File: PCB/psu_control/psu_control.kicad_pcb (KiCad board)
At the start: 4 copper layers, 100 x 70 mm, 113 parts, among them J1 Vin (10-25V), J10 Other 1 I2C, J11 Light Sensor Front, J12 Light Sensor Left, J13 Light Sensor Back, J14 Light Sensor Right, J15 RRC-PMM240, J16 RS232, J2 Vout (10-25V), J3 Vout (5V), J4 Vout (10-25V), J6 LED Strip, J7 Amplifier 2 I2C, J8 Amplifier 1 I2C, J9 Amplifier 2 I2C, M1 Fan, M2 Fan, Q1 SSM3J372R, Q2 IPD068P03L3GATMA1, Q3 T2N7002AK, Q4 AO4818B, SW1 Non-Momentary DPST, SW2 BUTTON, SW3 BUTTON, SW4 BUTTON, SW5 BUTTON, SW6 BUTTON, U1 LM810M3-4.63, U2 Teensy_LC, U3 INA220, U4 K7805-3AR3, U5 74HC14, U6 SN74LV1T34, U7 MAX3221E, U8 74LVC2G34

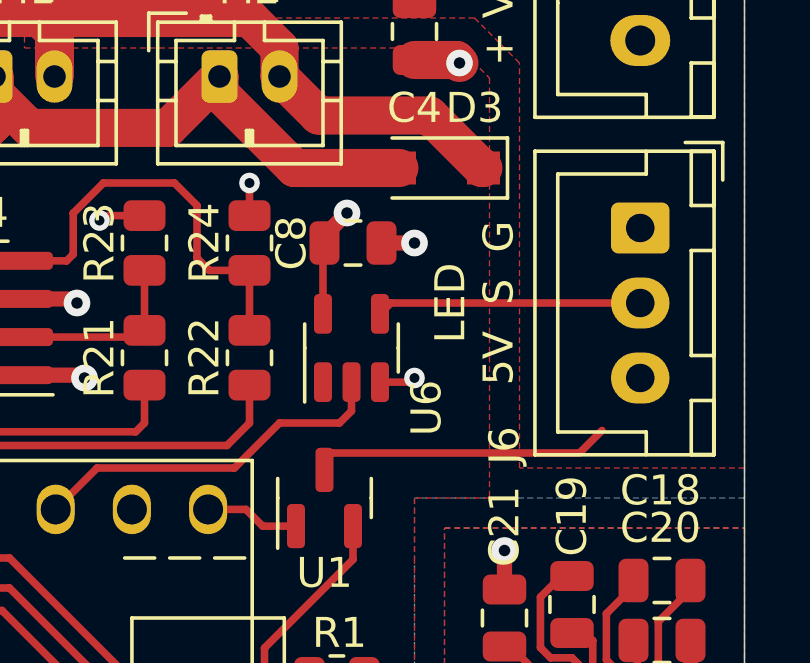
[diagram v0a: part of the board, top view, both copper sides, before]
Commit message: Add output resistor for the led strip (data).
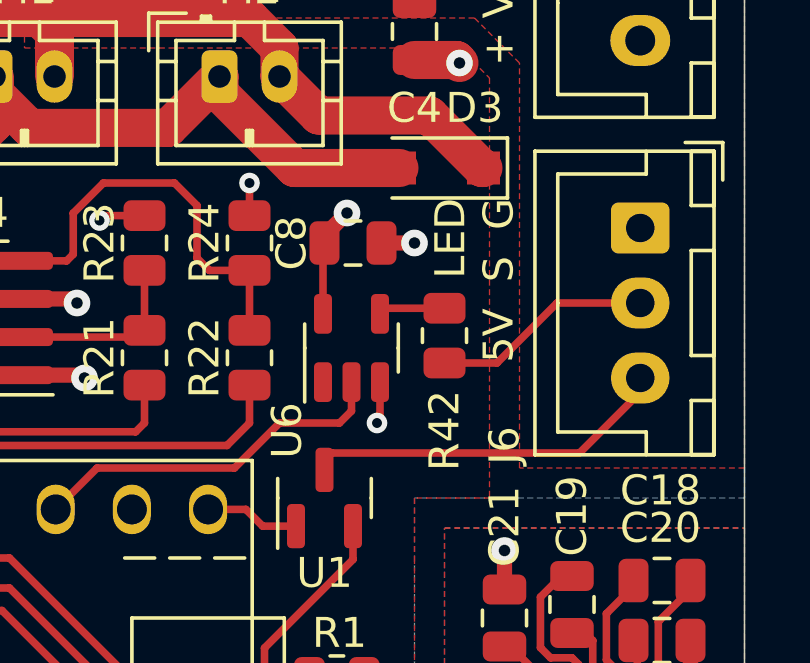
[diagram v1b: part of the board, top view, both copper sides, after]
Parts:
- added R42: 47, Resistor_SMD:R_0805_2012Metric, F.Cu at (105.0, 38.1)
- J9: value Amplifier 2 I2C -> Other 2 I2C
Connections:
- U6 pad 4: Net-(J6-Pad2) -> Net-(U6-Pad4)
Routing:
- net Net-(U6-Pad4): track 0.00 -> 2.35 mm
- net +5V: track 54.9 -> 57.1 mm
- net Net-(J6-Pad2): track 8.83 -> 7.35 mm

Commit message: Update gerbers
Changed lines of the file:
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@@
   (net 79 "Net-(J15-Pad5)")
   (net 80 "Net-(R7-Pad2)")
-  (net 81 "Net-(U6-Pad4)")
+  (net 81 "Net-(R42-Pad1)")
   (footprint "Resistor_SMD:R_0805_2012Metric" (layer "F.Cu")
     (at 106 20 180)
@@
       (net 2 "GND") (pinfunction "GND") (pintype "power_in"))
     (pad "4" smd roundrect (at 1.1375 0.95 90) (size 1.325 0.6) (layers "F.Cu" "F.Paste" "F.Mask") (roundrect_rratio 0.25)
-      (net 81 "Net-(U6-Pad4)") (pinfunction "Y") (pintype "output"))
+      (net 81 "Net-(R42-Pad1)") (pinfunction "Y") (pintype "output"))
     (pad "5" smd roundrect (at 1.1375 -0.95 90) (size 1.325 0.6) (layers "F.Cu" "F.Paste" "F.Mask") (roundrect_rratio 0.25)
       (net 7 "+5V") (pinfunction "VCC") (pintype "power_in"))
@@
     (fp_line (start -1 0.625) (end -1 -0.625) (layer "F.Fab") (width 0.1))
     (pad "1" smd roundrect (at -0.9125 0 270) (size 1.025 1.4) (layers "F.Cu" "F.Paste" "F.Mask") (roundrect_rratio 0.243902439)
-      (net 81 "Net-(U6-Pad4)") (pintype "passive"))
+      (net 81 "Net-(R42-Pad1)") (pintype "passive"))
     (pad "2" smd roundrect (at 0.9125 0 270) (size 1.025 1.4) (layers "F.Cu" "F.Paste" "F.Mask") (roundrect_rratio 0.243902439)
       (net 28 "Net-(J6-Pad2)") (pintype "passive"))
@@
   (segment (start 105 37.175) (end 103.0375 37.175) (width 0.254) (layer "F.Cu") (net 81))
   (segment (start 103.0375 37.175) (end 102.85 37.3625) (width 0.254) (layer "F.Cu") (net 81))
-  (segment (start 105 37.0875) (end 105.0875 37) (width 0.254) (layer "F.Cu") (net 81))
   (zone (net 2) (net_name "GND") (layer "F.Cu") (hatch edge 0.508)
     (connect_pads yes (clearance 0.508))

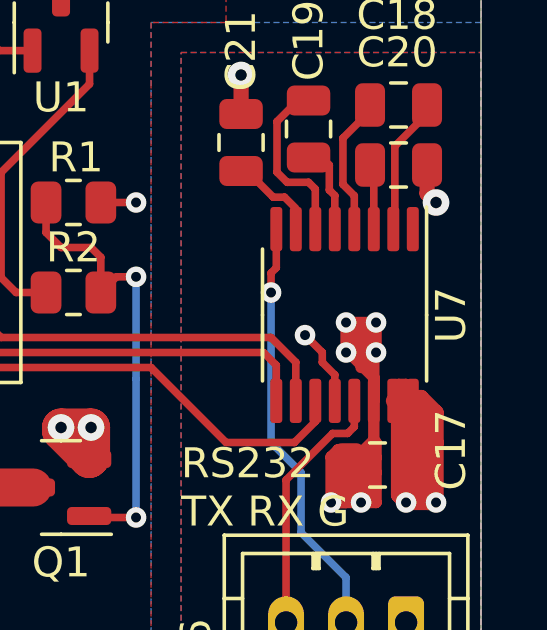
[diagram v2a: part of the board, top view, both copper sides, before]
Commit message: Change MAX3221E by SN65C3221E.
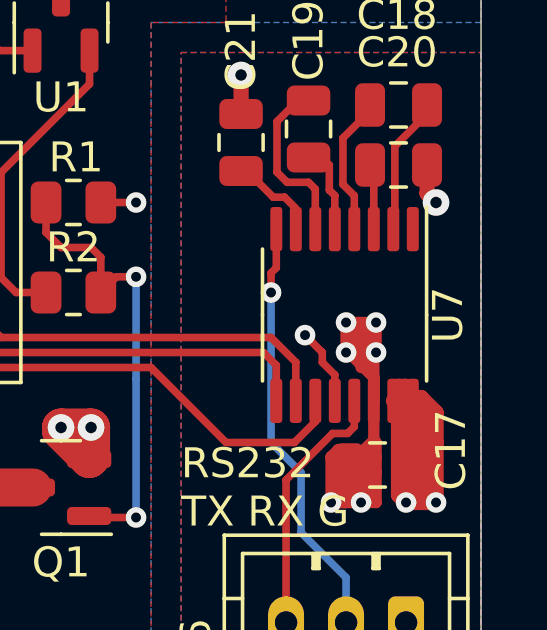
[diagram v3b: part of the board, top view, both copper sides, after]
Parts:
- U7: value MAX3221E -> SN65C3221E

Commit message: Fix PCBs.
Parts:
- removed J10: Other 1 I2C, Connector_JST:JST_PH_B3B-PH-K_1x03_P2.00mm_Vertical
- removed J3: Vout (5V), Connector_JST:JST_XH_B2B-XH-A_1x02_P2.50mm_Vertical
- removed J9: Other 2 I2C, Connector_JST:JST_PH_B3B-PH-K_1x03_P2.00mm_Vertical
- removed RV1: V12ZA1P, Varistor:RV_Disc_D7mm_W4mm_P5mm
- added C23: 100µF/35V, Capacitor_THT:CP_Radial_D6.3mm_P2.50mm, F.Cu at (109.8, 28.0)
- added C24: 10µF/25V, Capacitor_SMD:C_0805_2012Metric, F.Cu at (95.5, 36.0)
- added C25: 0.1µF/25V, Capacitor_SMD:C_0805_2012Metric, F.Cu at (68.5, 68.0)
- added C26: 0.1µF/25V, Capacitor_SMD:C_0805_2012Metric, F.Cu at (71.5, 68.0)
- added C27: 0.1µF/25V, Capacitor_SMD:C_0805_2012Metric, F.Cu at (65.5, 68.0)
- added C28: 0.1µF/25V, Capacitor_SMD:C_0805_2012Metric, F.Cu at (62.5, 68.0)
- added C29: 0.1µF/25V, Capacitor_SMD:C_0805_2012Metric, F.Cu at (74.5, 68.0)
- added C30: 0.1µF/25V, Capacitor_SMD:C_0805_2012Metric, F.Cu at (77.5, 68.0)
- added C31: 22μF/10V, Capacitor_SMD:C_0805_2012Metric, F.Cu at (109.5, 23.5)
- added D6: SMAJ9.0A-13-F, Diode_SMD:D_SMA, F.Cu at (95.5, 42.0)
- added L2: 22µH (NS12575T220MN), t-top:NS12575T220MN, F.Cu at (100.0, 22.5)
- added REF**: MountingHole_3.2mm_M3, MountingHole:MountingHole_3.2mm_M3, F.Cu at (50.0, 73.5)
- added REF**: MountingHole_3.2mm_M3, MountingHole:MountingHole_3.2mm_M3, F.Cu at (70.0, 73.5)
- Q4: value AO4818B -> DMG9926USD
- R16, R17, R19, R20: moved to B.Cu
- moved R24 28.2 mm to (71.1, 41.5), turned to 180 degrees
- moved R23 25.7 mm to (71.1, 44.5), turned to 180 degrees
- moved C5 24.9 mm to (42.0, 30.8)
- moved D1 24.4 mm to (102.5, 32.2), turned to 0 degrees
- moved Q4 23.8 mm to (65.0, 41.5), turned to 90 degrees
- moved R22 23.6 mm to (75.1, 41.5), turned to 180 degrees
- moved C11 21.9 mm to (55.0, 52.5)
- moved R30 21.8 mm to (50.9, 52.5)
- moved D2 21.8 mm to (85.0, 35.0)
- moved R27 21.6 mm to (46.9, 52.5)
- moved R21 20.7 mm to (75.1, 44.5), turned to 180 degrees
- moved C4 19.5 mm to (84.5, 27.5)
- moved R31 17.5 mm to (50.9, 55.5), turned to 0 degrees
- moved C12 17.5 mm to (55.0, 55.5), turned to 0 degrees
- moved C13 17.4 mm to (55.0, 58.5), turned to 0 degrees
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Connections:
- C10 pad 2: GND -> Net-(D3-Pad2)
- C4 pad 1: +5V -> Net-(C4-Pad1)
- C9 pad 1: Net-(C10-Pad1) -> Net-(C4-Pad1)
- R17 pad 1: +5V -> Net-(C4-Pad1)
- U2 pad 11: /BUTTON_VOLUME_DOWN -> /BUTTON_START
- U2 pad 12: /BUTTON_VOLUME_UP -> /POWER_SWITCH
- U2 pad 4: /POWER_SWITCH -> /BUTTON_VOLUME_DOWN
- U2 pad 9: /BUTTON_START -> /BUTTON_VOLUME_UP
- U4 pad 9: +5V -> Net-(C4-Pad1)
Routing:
- net +5V: track 57.1 -> 117.5 mm, vias 5 -> 4
- net Net-(C4-Pad1): track 0.00 -> 41.1 mm
- net Net-(D3-Pad2): track 25.5 -> 53.6 mm
- net Net-(C6-Pad1): track 2.60 -> 29.1 mm
- net /POWER_SWITCH: track 34.6 -> 9.40 mm, vias 1 -> 0
- net Net-(R27-Pad2): track 5.69 -> 26.4 mm
- net Net-(R34-Pad2): track 6.69 -> 22.0 mm
- net Net-(R15-Pad2): track 7.02 -> 21.1 mm
- net Net-(R28-Pad2): track 8.41 -> 21.9 mm
- net Net-(R33-Pad2): track 7.05 -> 19.4 mm
- net /Actuators/BUZZER_PWM: track 18.1 -> 6.00 mm, vias 0 -> 1
- net Net-(R29-Pad2): track 7.05 -> 19.2 mm
- net +3.3V: track 57.0 -> 45.2 mm
- net GND: track 94.5 -> 106.1 mm, vias 31 -> 35
- net Net-(J15-Pad5): track 10.6 -> 21.6 mm, vias 1 -> 3
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- added copper zone on In2.Cu, net GND
- removed copper zone on F.Cu, net +5V
- removed copper zone on In2.Cu, net +5V
- removed copper zone on F.Cu, net Net-(C6-Pad1)
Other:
- board text added: "5V S G"
- board text added: "G SCL SDA"
- board text added: "LED"
- board text added: "RRC- PMM240"
- board text removed: "5V + Vout -"
- board text removed: "LED 5V S G"
- board text removed: "RRC-PMM240"
- board text removed: "SDA SCL G"

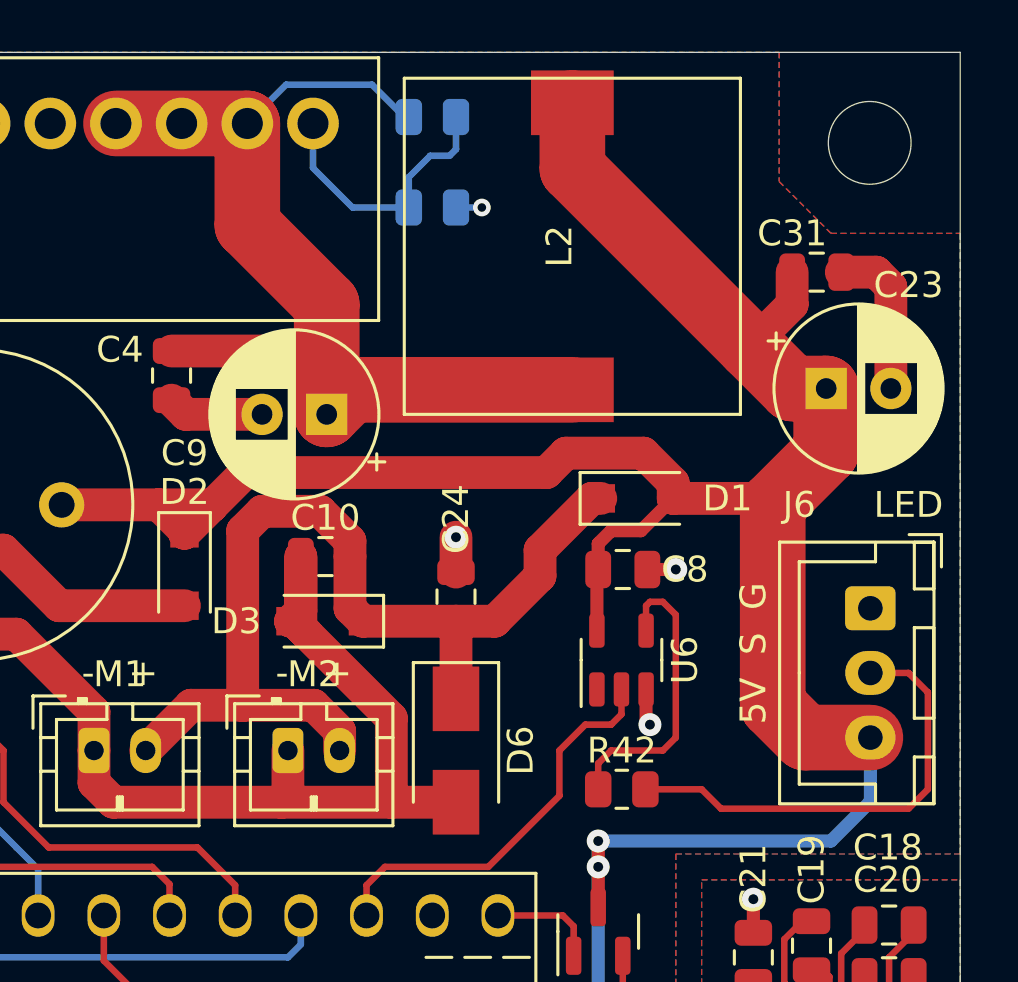
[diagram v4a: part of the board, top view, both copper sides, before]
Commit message: Add a PI filter to buck_boost. Fix ringing for other PI filters.
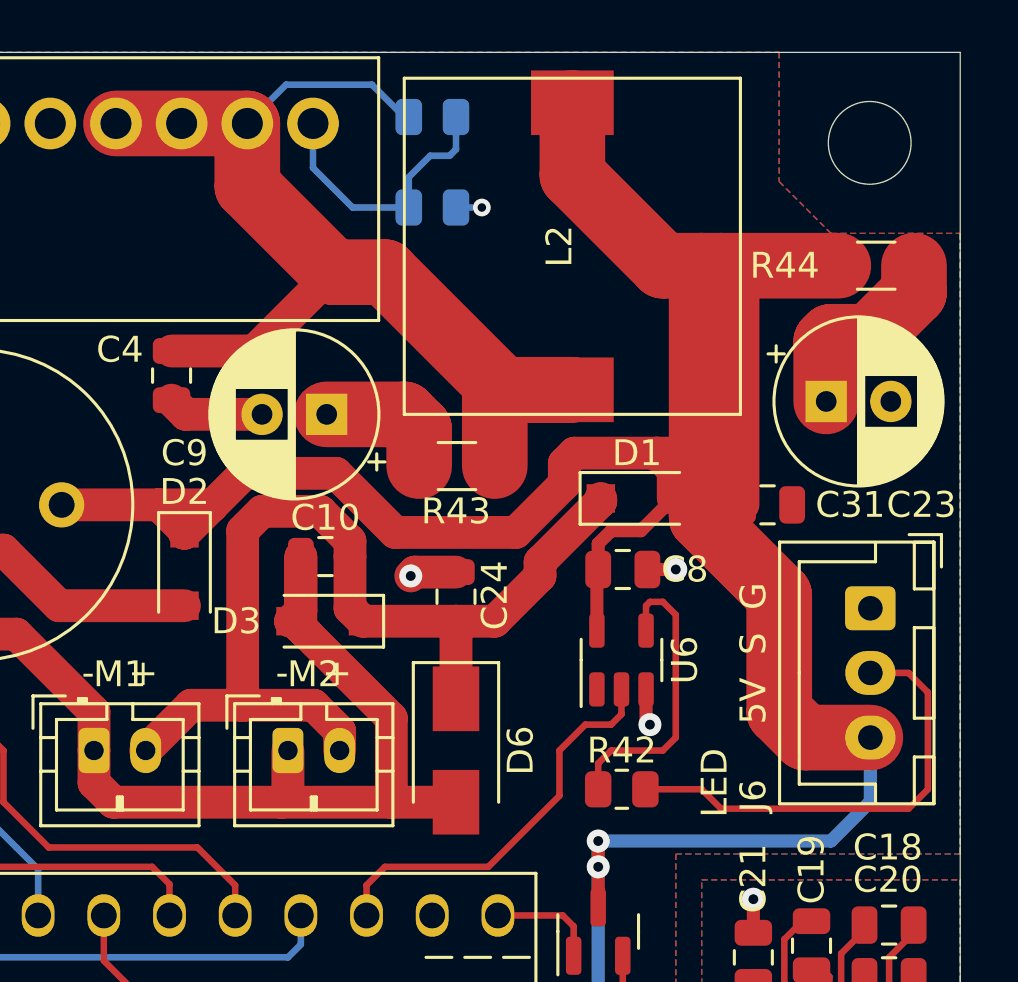
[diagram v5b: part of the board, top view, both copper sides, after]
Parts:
- added R43: 0, Resistor_SMD:R_1206_3216Metric, F.Cu at (95.5, 31.0)
- added R44: 0, Resistor_SMD:R_1206_3216Metric, F.Cu at (111.8, 23.2)
- moved C31 9.20 mm to (107.5, 32.5)
- moved C23 0.50 mm to (109.8, 28.5)
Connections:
- C23 pad 1: +5V -> Net-(C23-Pad1)
- C9 pad 1: Net-(C4-Pad1) -> Net-(C9-Pad1)
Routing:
- net +5V: track 117.5 -> 127.9 mm
- net Net-(C23-Pad1): track 0.00 -> 7.53 mm
- net GND: track 106.1 -> 100.5 mm
- net Net-(C9-Pad1): track 0.00 -> 5.24 mm
- net Net-(C4-Pad1): track 41.1 -> 43.9 mm
